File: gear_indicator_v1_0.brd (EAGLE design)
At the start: 55.5 x 63.5 mm, 28 parts, among them IC1 NE555, IC2 74ALS08N, IC3 74ALS04N, IC4 7805TV, T1 2N3904, T2 2N3904, T3 2N3904

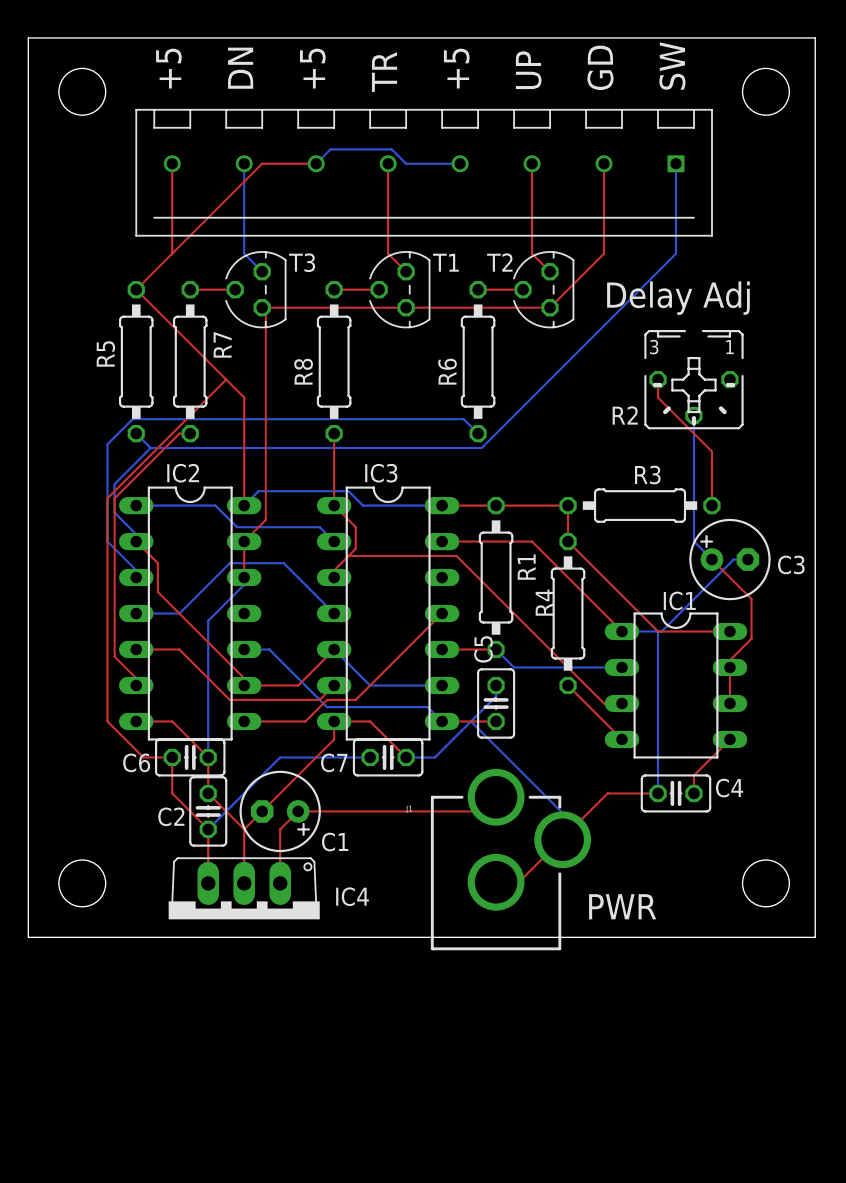
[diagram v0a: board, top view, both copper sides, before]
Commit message: Fixed tie to ground for unused logic gates Added low pass filter on switch input
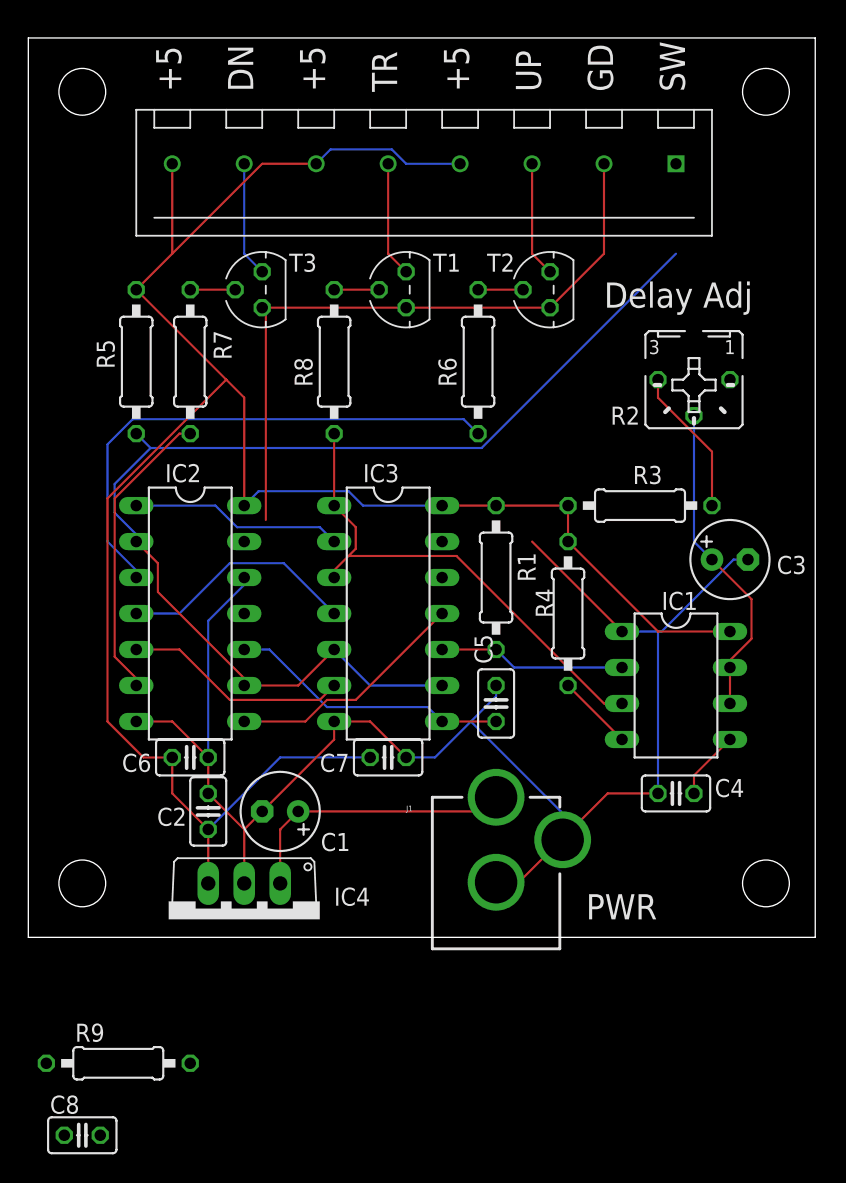
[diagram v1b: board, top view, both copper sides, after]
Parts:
- added C8: 0.1, resistor:C025-025X050
- added R9: 1K, resistor:0207/10
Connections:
- new net N$17: J2.1, R9.1
- net GND: now also C8.2, IC2.11, IC3.12; no longer IC2.12, IC2.13, IC3.13
- net SWITCH: now also C8.1, R9.2; no longer J2.1
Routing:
- net GND: track 169.8 -> 158.2 mm
- net SWITCH: track 88.2 -> 81.9 mm
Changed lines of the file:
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@@
 <attribute name="VALUE" x="23.114" y="9.906" size="1.27" layer="27" ratio="10"/>
 </element>
+<element name="R9" library="resistor" package="0207/10" value="1K" x="6.35" y="-8.89"/>
+<element name="C8" library="resistor" package="C025-025X050" value="0.1" x="3.81" y="-13.97"/>
 </elements>
 <signals>
@@
 <contactref element="C4" pad="2"/>
 <contactref element="C5" pad="2"/>
-<contactref element="IC3" pad="13"/>
-<contactref element="IC2" pad="13"/>
-<contactref element="IC2" pad="12"/>
 <contactref element="J1" pad="GND"/>
 <contactref element="J1" pad="GNDBREAK"/>
@@
 <wire x1="33.02" y1="4.064" x2="33.02" y2="3.89" width="0.1524" layer="1"/>
 <wire x1="37.592" y1="6.858" x2="37.72" y2="6.89" width="0.1524" layer="1"/>
-<wire x1="35.56" y1="27.94" x2="29.21" y2="27.94" width="0.1524" layer="1"/>
 <wire x1="41.91" y1="21.59" x2="35.56" y2="27.94" width="0.1524" layer="1"/>
 <wire x1="49.784" y1="26.67" x2="50.8" y2="26.67" width="0.1524" layer="16"/>
@@
 <wire x1="15.24" y1="7.62" x2="15.24" y2="3.81" width="0.1524" layer="1"/>
 <wire x1="16.51" y1="8.89" x2="15.24" y2="7.62" width="0.1524" layer="1"/>
-<wire x1="15.24" y1="27.94" x2="15.24" y2="25.4" width="0.1524" layer="1"/>
 <wire x1="12.7" y1="12.7" x2="12.7" y2="10.16" width="0.1524" layer="1"/>
 <wire x1="10.16" y1="15.24" x2="7.62" y2="15.24" width="0.1524" layer="1"/>
 <wire x1="12.7" y1="12.7" x2="10.16" y2="15.24" width="0.1524" layer="1"/>
-<wire x1="15.24" y1="24.892" x2="15.24" y2="25.4" width="0.1524" layer="16"/>
 <wire x1="12.7" y1="22.352" x2="15.24" y2="24.892" width="0.1524" layer="16"/>
 <wire x1="12.7" y1="12.7" x2="12.7" y2="22.352" width="0.1524" layer="16"/>
@@
 <wire x1="16.51" y1="8.89" x2="21.59" y2="13.97" width="0.1524" layer="1"/>
 <wire x1="16.764" y1="29.464" x2="16.764" y2="44.45" width="0.1524" layer="1"/>
-<wire x1="15.24" y1="27.94" x2="16.764" y2="29.464" width="0.1524" layer="1"/>
 <wire x1="16.764" y1="44.45" x2="16.51" y2="44.45" width="0.1524" layer="1"/>
 <wire x1="37.592" y1="8.89" x2="37.592" y2="7.112" width="0.1524" layer="16"/>
 <wire x1="31.242" y1="15.24" x2="37.592" y2="8.89" width="0.1524" layer="16"/>
 <wire x1="37.592" y1="7.112" x2="37.72" y2="6.89" width="0.1524" layer="16"/>
+<contactref element="IC2" pad="11"/>
+<contactref element="IC3" pad="12"/>
+<contactref element="C8" pad="2"/>
+<wire x1="35.56" y1="27.94" x2="29.21" y2="25.4" width="0" layer="19" extent="1-1"/>
+<wire x1="15.24" y1="22.86" x2="15.24" y2="24.892" width="0" layer="19" extent="16-16"/>
+<wire x1="16.764" y1="29.464" x2="15.24" y2="24.892" width="0" layer="19" extent="1-16"/>
+<wire x1="5.08" y1="-13.97" x2="15.24" y2="3.81" width="0" layer="19" extent="1-1"/>
 </signal>
 <signal name="N$2">
@@
 <contactref element="IC3" pad="9"/>
 <contactref element="IC2" pad="9"/>
-<contactref element="J2" pad="1"/>
 <wire x1="19.05" y1="17.78" x2="15.24" y2="17.78" width="0.1524" layer="1"/>
 <wire x1="21.59" y1="20.32" x2="19.05" y2="17.78" width="0.1524" layer="1"/>
 <wire x1="24.13" y1="17.78" x2="29.21" y2="17.78" width="0.1524" layer="16"/>
 <wire x1="21.59" y1="20.32" x2="24.13" y2="17.78" width="0.1524" layer="16"/>
-<wire x1="45.72" y1="48.26" x2="45.72" y2="54.61" width="0.1524" layer="16"/>
 <wire x1="32.004" y1="34.544" x2="45.72" y2="48.26" width="0.1524" layer="16"/>
 <wire x1="8.636" y1="34.544" x2="32.004" y2="34.544" width="0.1524" layer="16"/>
@@
 <wire x1="9.144" y1="26.416" x2="9.144" y2="24.384" width="0.1524" layer="1"/>
 <wire x1="7.62" y1="27.94" x2="9.144" y2="26.416" width="0.1524" layer="1"/>
+<contactref element="R9" pad="2"/>
+<contactref element="C8" pad="1"/>
+<wire x1="11.43" y1="-8.89" x2="15.24" y2="17.78" width="0" layer="19" extent="1-1"/>
+<wire x1="2.54" y1="-13.97" x2="11.43" y2="-8.89" width="0" layer="19" extent="1-1"/>
 </signal>
 <signal name="N$8">
@@
 <wire x1="16.51" y1="46.99" x2="15.24" y2="48.26" width="0.1524" layer="16"/>
 </signal>
+<signal name="N$17">
+<contactref element="J2" pad="1"/>
+<contactref element="R9" pad="1"/>
+<wire x1="1.27" y1="-8.89" x2="45.72" y2="54.61" width="0" layer="19" extent="1-1"/>
+</signal>
 </signals>
-<errors>
-</errors>
 </board>
 </drawing>

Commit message: layout tweaks
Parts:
- added LED1: Power, dp_devices:LED-3MM
- added R10: 220, resistor:0207/7
- C3: device rcl:E2,5-6 -> rcl:E3,5-10
- R1, R3, R4, R5, R6, R7, R8, R9: device resistor:0207/10 -> resistor:0207/7
- moved R9 74.4 mm to (50.8, 50.8), turned to 270 degrees
- moved C8 71.9 mm to (41.9, 47.0), turned to 180 degrees
- moved C7 23.2 mm to (29.2, 35.6), turned to 90 degrees
- moved C6 23.2 mm to (15.2, 35.6), turned to 90 degrees
- moved J1 8.91 mm to (41.9, -3.17)
- moved C3 8.52 mm to (41.9, 30.5), turned to 180 degrees
- moved R3 8.52 mm to (39.4, 38.1)
- moved C4 6.35 mm to (50.8, 14.0), turned to 270 degrees
- moved R4 3.59 mm to (35.6, 25.4)
- moved IC1 2.84 mm to (43.2, 19.1)
- moved R2 2.84 mm to (49.5, 38.1)
- moved C2 1.42 mm to (11.4, 8.26), turned to 180 degrees
- moved T1 1.27 mm to (25.4, 45.7)
- moved T3 1.27 mm to (15.2, 45.7)
- moved C1 1.27 mm to (17.8, 10.2), turned to 90 degrees
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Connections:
- new net N$16: LED1.K, R10.2
- net GND: now also R10.1
- net VCC: now also LED1.A
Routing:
- net GND: track 158.2 -> 0.00 mm
- net VCC: track 149.1 -> 186.9 mm
- net N$12: track 20.1 -> 32.0 mm
- net SWITCH: track 81.9 -> 92.2 mm
- net N$2: track 22.6 -> 30.4 mm
- net OUT: track 35.0 -> 42.5 mm
- net N$1: track 10.5 -> 3.81 mm
- net N$16: track 0.00 -> 5.61 mm
- net N$17: track 0.00 -> 5.08 mm
- net N$9: track 21.1 -> 25.8 mm
- net N$3: track 5.39 -> 8.67 mm
- net N$6: track 16.9 -> 15.0 mm
- net TRG: track 13.2 -> 11.4 mm
- net N$13: track 3.18 -> 1.91 mm
- net N$10: track 3.18 -> 1.91 mm
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- added copper zone on layer 16, net GND
